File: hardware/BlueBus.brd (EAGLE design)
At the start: 64.4 x 66 mm, 46 parts

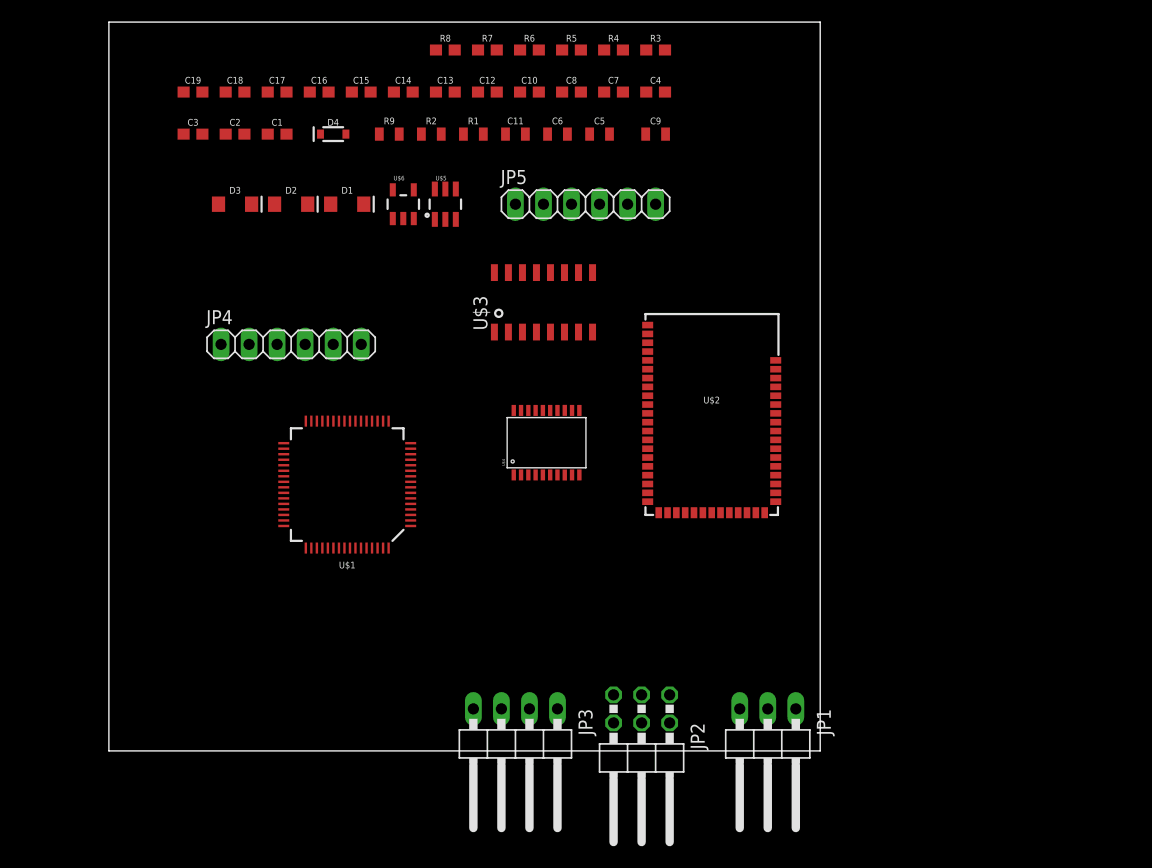
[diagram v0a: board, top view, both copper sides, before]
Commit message: [IMP] hardware: Finalize Schematic & Rev 1 board * Finish Schematic * Finalize board layout for rev 1 board
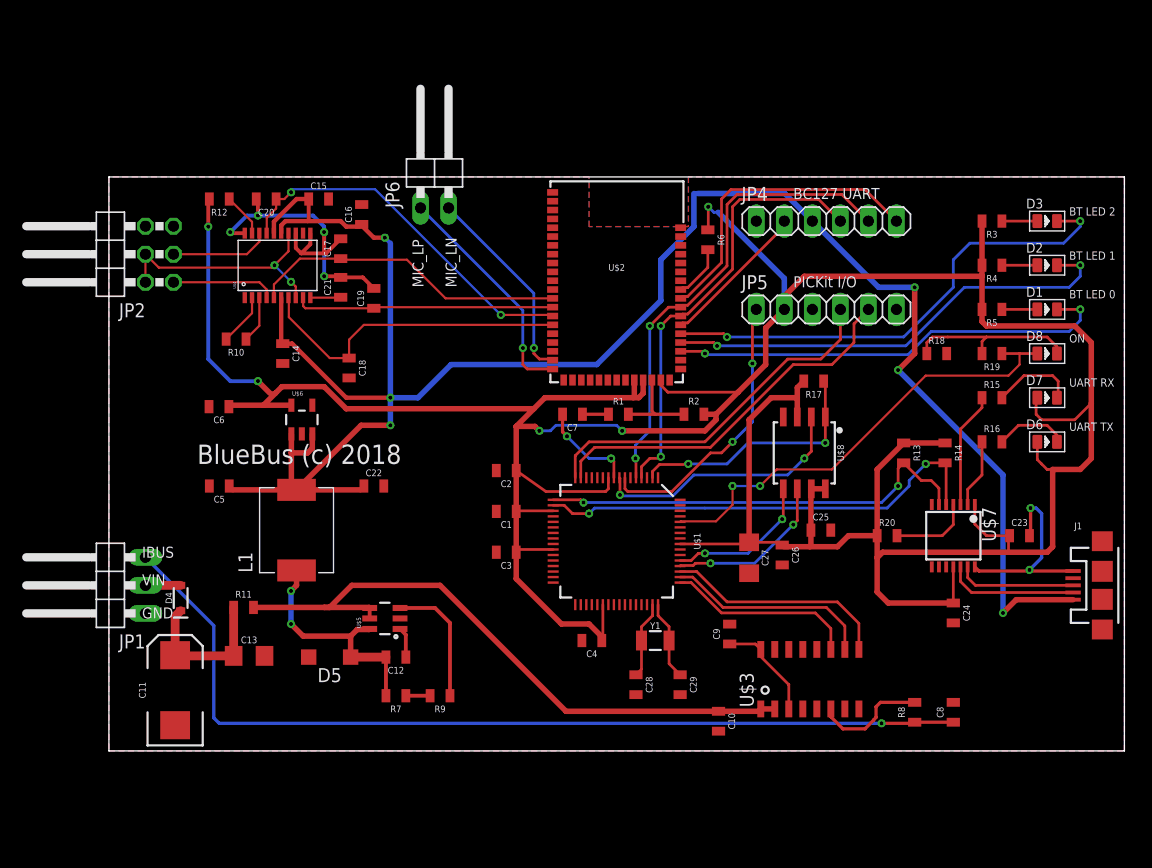
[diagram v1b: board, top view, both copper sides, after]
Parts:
- removed FRAME4: FRAME-LETTER, Frame:DUMMY
- removed JP3: (no value), pinhead:1X04/90
- added C20, C21: 0.47uF, Passives:0805
- added C22: 22uF, Passives:0805
- added C23, C24, C25, C26: 0.1uF, Passives:0805
- added C27: 10uF, Passives:1206
- added C28, C29: 18pF, Passives:0805
- added D5: 2A/30V, Passives:SOD123
- added D6: RED-0805, Seeed-LED:LED-0805
- added D7, D8: GREEN-0805, Seeed-LED:LED-0805
- added FRAME3: FRAME-LETTER, Frame:DUMMY
- added J1: (no value), SparkFun-Connectors:USB-MICROB
- added JP6: MIC_IN, pinhead:1X02/90
- added L1: 4.7uH, Passives:7.7MMX6.7MM
- added R10: 25k, Passives:0805
- added R11, R13, R14: 100k, Passives:0805
- added R12, R20: 10k, Passives:0805
- added R15, R16: 1k, Passives:0805
- added R17: 5.1k, Passives:0805
- added R18: 2k, Passives:0805
- added R19: 36k, Passives:0805
- added U$7: MCP2221A, ICs:TSSOP14
- added U$8: 512kB, ICs:SOIC-8
- added Y1: 32.768kHz, SparkFun-Clocks:CRYSTAL-SMD-3.2X1.5MM
- C1, C12, C14, C2, C3, C4, C7: device SparkFun-Capacitors:0603 -> Passives:0805
- C10: value 10nF -> 47nF; device SparkFun-Capacitors:0603 -> Passives:0805
- C11: value 10uF -> 100uF; device SparkFun-Capacitors:0805 -> Passives:EIA7343
- C13: value 0.1uF -> 10uF; device SparkFun-Capacitors:0603 -> Passives:1206
- C15, C16: value 47nF -> 0.1uF; device SparkFun-Capacitors:0603 -> Passives:0805
- C17, C18, C19: value 47nF -> 0.47uF; device SparkFun-Capacitors:0603 -> Passives:0805
- C5, C6: value 1.0uF -> 0.1uF; device SparkFun-Capacitors:0805 -> Passives:0805
- C8: value 100pF -> 0.1uF; device SparkFun-Capacitors:0603 -> Passives:0805
- C9: value 47uF/6.3V -> 2.2uF; device SparkFun-Capacitors:0805 -> Passives:0805
- D1: value BLUE -> RED-0805; device SparkFun-LED:LED-1206 -> Seeed-LED:LED-0805
- D2: value GREEN -> GREEN-0805; device SparkFun-LED:LED-1206 -> Seeed-LED:LED-0805
- D3: value RED -> CLEAR-BLUE-0805; device SparkFun-LED:LED-1206 -> Seeed-LED:LED-0805
- JP1: value (none) -> IBUS/VIN
- JP2: value (none) -> SPKR_OUT
- JP4: value (none) -> BT_FTDI
- JP5: value (none) -> MCU_PRGM
- R1, R2: device SparkFun-Resistors:0805 -> Passives:0805
- R3, R4, R5, R6, R7, R8: device SparkFun-Resistors:0603 -> Passives:0805
- R9: device Resistors:0805 -> Passives:0805
- U$4: value (none) -> TPA6012A2
- U$6: value (none) -> XC6210
- moved D3 73.6 mm to (85.0, 48.0)
- moved R8 73.5 mm to (73.0, 3.50), turned to 90 degrees
- moved D2 68.7 mm to (85.0, 44.0)
- moved JP2 67.2 mm to (-0.50, 45.0), turned to 90 degrees
- moved C8 66.0 mm to (76.5, 3.50), turned to 90 degrees
- moved D1 64.1 mm to (85.0, 40.0)
- moved JP1 62.0 mm to (-0.50, 15.0), turned to 90 degrees
- moved C10 59.5 mm to (55.2, 2.69), turned to 270 degrees
- moved R7 59.1 mm to (26.0, 5.00), turned to 180 degrees
- moved C11 59.1 mm to (6.00, 5.50), turned to 90 degrees
- moved C13 54.1 mm to (12.7, 8.61)
- moved C12 51.9 mm to (26.0, 8.50), turned to 180 degrees
- moved R9 51.1 mm to (30.0, 5.00), turned to 180 degrees
- moved C4 50.0 mm to (43.8, 10.0), turned to 180 degrees
- moved JP4 49.8 mm to (65.0, 48.0)
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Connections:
- net BT_UART_CTS renamed BT_UCTS
- net BT_UART_RTS renamed BT_URTS
- net N$1 renamed BT_VBAT_2
- net N$10 renamed FB_RES
- net N$12 renamed FB
- net N$3 renamed BT_RESET
- removed net BT_UART_RX: JP4.5, U$2.42
- removed net BT_UART_TX: JP4.4, U$2.41
- removed net IBUS_UART_RX: U$3.10
- removed net IBUS_UART_STA: U$3.9
- removed net IBUS_UART_TX: U$3.11
- removed net MIC_BIAS: U$2.17
- removed net MIC_RN: JP3.3, U$2.18
- removed net MIC_RP: JP3.1, U$2.19
- removed net N$11: C18.1, U$4.10
- removed net N$6: D1.C, U$2.38
- removed net N$7: D3.C, U$2.39
- removed net N$8: D3.A, R3.1
- removed net N$9: C10.1, U$5.1
- removed net SPKR_LN: U$2.13
- removed net SPKR_OUT_LN: JP2.2, U$4.8
- removed net SPKR_OUT_RN: JP2.4, U$4.14
- removed net VCAP: U$1.56
- removed net VCC: U$3.16
- new net BS: C12.1, U$5.1
- new net BT_URX: JP4.5, U$1.5, U$2.42
- new net BT_UTX: JP4.4, U$1.4, U$2.41
- new net BT_VBAT: R1.2, R2.1, U$2.32
- new net BYPASS: C21.1, U$4.10
- new net CRYSTAL_IN: C28.1, U$1.47, Y1.P$1
- new net CRYSTAL_OUT: C29.1, U$1.48, Y1.P$2
- new net EE_CS: R17.1, U$1.2, U$8.1
- new net EE_SCK: U$1.52, U$8.6
- new net EE_SI: U$1.53, U$8.5
- new net EE_SO: U$1.8, U$8.2
- new net GAIN0: R10.2, U$4.2
- new net GAIN1: R10.1, U$4.3
- new net IBUS_IN: R8.2, U$3.6
- new net IBUS_URX: U$1.50, U$3.10
- new net IBUS_USTA: U$1.51, U$3.9
- new net IBUS_UTX: U$1.49, U$3.11
- new net LED0: D1.-, U$2.37
- new net LED1: D2.-, U$2.38
- new net LED2: D3.-, U$2.39
- new net MCP_LED0: R16.1, U$7.2
- new net MCP_LED1: R15.1, U$7.3
- new net MCP_RESET: R20.2, U$7.4
- new net N$1: D3.+, R3.1
- new net N$3: D1.+, R5.1
- new net ON_LED: D8.+, R19.1, U$1.60
- new net ON_LED_RES: D8.-, R18.1, R19.2
- new net SHDN: R12.1, U$4.19
- new net SPKR_OUT_NEG: JP2.2, JP2.4, U$4.14, U$4.8
- new net SW: C12.2, D5.C, L1.P$1, R7.2, U$5.6
- new net SYS_URX: R14.2, U$1.18, U$7.5
- new net SYS_USB_DN: J1.D-, U$7.12
- new net SYS_USB_DP: J1.D+, U$7.13
- new net SYS_UTX: R13.2, U$1.17, U$7.6
- new net VTR: C9.1, U$3.16, U$3.3
- net 3.3V: now also C23.1, C24.1, C25.1, C26.1, C27.1, D6.+, D7.+, R12.2, R13.1, R14.1, R17.2, R20.1, U$1.56, U$2.30, U$7.1, U$7.11, U$8.3, U$8.7, U$8.8; no longer D1.A, D2.A, R4.1, R5.1, U$2.32
- net 5V: now also C15.1, C16.1, C22.1, J1.VBUS, L1.P$2; no longer C10.2, C12.1, C13.1, R7.2, U$5.6
- net GND: now also C10.2, C11.C, C20.2, C21.2, C22.2, C23.2, C24.2, C25.2, C26.2, C27.2, C28.2, C29.2, D5.A, J1.GND, R18.2, U$7.14, U$8.4; no longer C11.2, C12.2, U$3.2
- net IBUS: now also C8.1; no longer D4.A, D4.C
- net MIC_LN: now also JP6.2; no longer JP3.4
- net MIC_LP: now also JP6.1; no longer JP3.2
- net N$2: now also D2.+, R4.1; no longer R1.2, R2.1, U$2.30
- net N$4: now also D7.-, R15.2; no longer C8.1, R8.2, U$3.6
- net N$5: now also D6.-, R16.2; no longer D2.C, U$2.37
- net SPKR_IN_LN: now also C17.1, U$2.13; no longer C15.1
- net SPKR_IN_LP: now also C19.1; no longer C17.1
- net SPKR_IN_RN: now also C20.1; no longer C19.1
- net SPKR_IN_RP: now also C18.1; no longer C16.1
- net VIN: now also C10.1, C11.A, C13.1, D4.A, D4.C, R11.1, R11.2, U$3.2, U$5.4; no longer C11.1, C9.1
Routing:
- net 3.3V: track 0.00 -> 337.2 mm, vias 0 -> 5
- net 5V: track 0.00 -> 187.6 mm, vias 0 -> 6
- net IBUS: track 0.00 -> 84.4 mm, vias 0 -> 1
- net VIN: track 0.00 -> 75.4 mm
- net GND: track 0.00 -> 59.5 mm, vias 0 -> 8
- net LED2: track 0.00 -> 44.5 mm, vias 0 -> 2
- net BT_URX: track 0.00 -> 43.3 mm, vias 0 -> 2
- net LED1: track 0.00 -> 42.0 mm, vias 0 -> 2
- net ON_LED: track 0.00 -> 41.9 mm, vias 0 -> 2
- net SYS_URX: track 0.00 -> 41.8 mm, vias 0 -> 2
- net LED0: track 0.00 -> 40.7 mm, vias 0 -> 2
- net BT_UTX: track 0.00 -> 40.1 mm, vias 0 -> 2
- net SYS_UTX: track 0.00 -> 39.9 mm, vias 0 -> 2
- net MCU_PGC: track 0.00 -> 34.2 mm
- net SPKR_IN_RN: track 0.00 -> 33.8 mm, vias 0 -> 2
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- added copper zone on layer 1, net GND
- added copper zone on layer 16, net GND
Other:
- board size 64.4 x 66 mm -> 92 x 52 mm
- board text added: "BC127 UART"
- board text added: "BT LED 0"
- board text added: "BT LED 1"
- board text added: "BT LED 2"
- board text added: "BlueBus (c) 2018"
- board text added: "GND"
- board text added: "IBUS"
- board text added: "MIC_LN"
- board text added: "MIC_LP"
- board text added: "ON"
- board text added: "PICKit I/O"
- board text added: "UART RX"
- board text added: "UART TX"
- board text added: "VIN"

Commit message: [IMP] hardware: Minor updates to design * Increase trace size to 0.22mm minimum * Increase all power traces to .5mm minimum * Add silkscreen goodies and name parts directly on PCB * Ensure all nets are named aptly
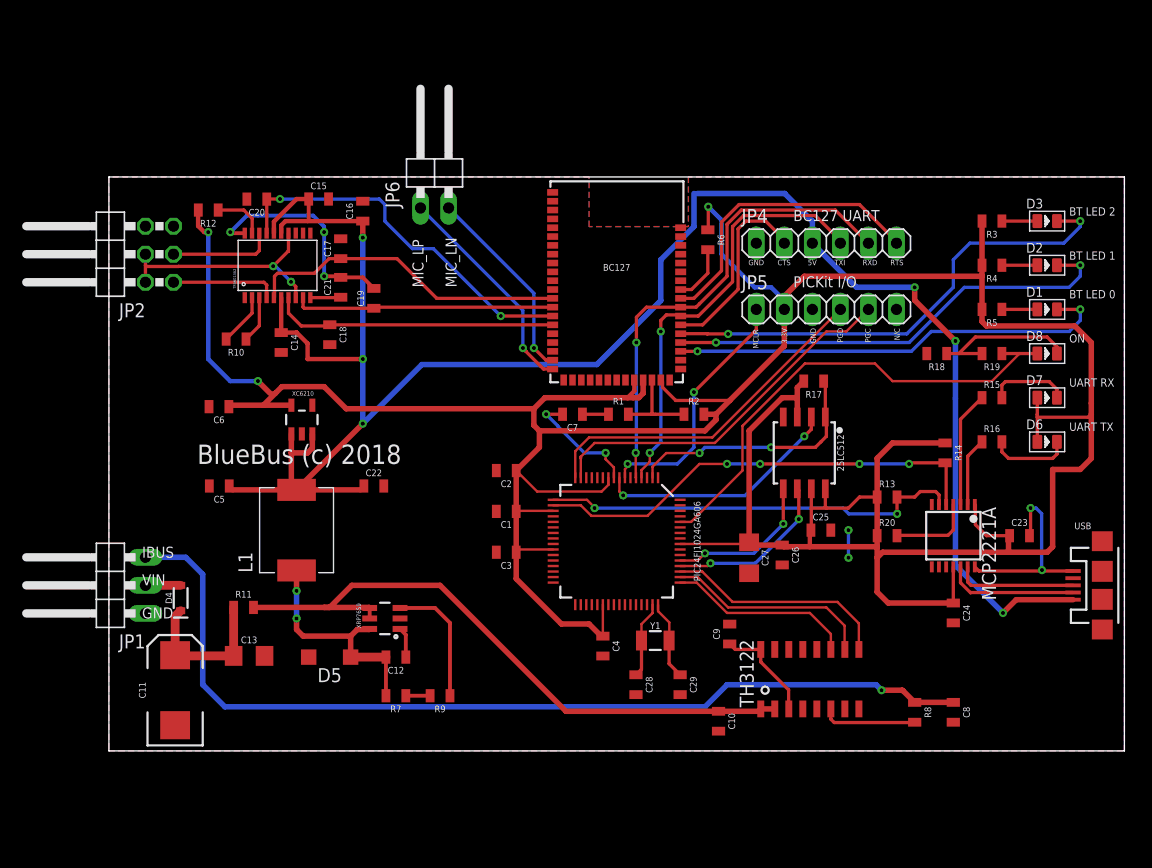
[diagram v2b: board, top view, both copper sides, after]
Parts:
- moved R13 4.27 mm to (70.5, 23.0), turned to 0 degrees
- moved C18 3.49 mm to (20.0, 37.7)
- moved JP4 2.00 mm to (65.0, 46.0)
- moved R12 1.41 mm to (9.00, 49.0)
- moved C4 1.12 mm to (44.8, 9.50), turned to 270 degrees
- moved C14 1.01 mm to (15.6, 37.0)
- moved C20 0.85 mm to (13.4, 50.0)
- moved C16 0.32 mm to (23.0, 48.9)
- turned C8 to 270 degrees
- turned R18 to 180 degrees
- turned R8 to 270 degrees
- renumbered J1 to USB, U$1 to PIC24FJ1024GA606, U$2 to BC127, U$3 to TH3122, U$4 to TPA6013A2, U$5 to XRP7659, U$6 to XC6210, U$7 to MCP2221A, U$8 to 25LC512
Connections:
- net N$1 renamed LED2_RES
- net N$2 renamed LED1_RES
- net N$3 renamed LED0_RES
- net N$4 renamed MCP_LED1_RES
- net N$5 renamed MCP_LED0_RES
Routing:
- net GND: track 59.5 -> 51.7 mm, vias 8 -> 9
- net 5V: track 187.6 -> 183.1 mm
- net BT_UCTS: track 13.6 -> 17.5 mm
- net SPKR_IN_RP: track 29.4 -> 25.9 mm
- net 3.3V: track 337.2 -> 340.5 mm, vias 5 -> 3
- net MCU_MCLR: track 25.6 -> 22.8 mm
- net ON_LED: track 41.9 -> 44.0 mm, vias 2 -> 0
- net ON_LED_RES: track 15.6 -> 13.7 mm
- net IBUS: track 84.4 -> 86.1 mm
- net IBUS_IN: track 10.3 -> 8.66 mm
- net SYS_UTX: track 39.9 -> 38.3 mm
- net MCU_PGD: track 33.1 -> 31.7 mm
- net EE_SO: track 23.7 -> 22.4 mm
- net BT_URTS: track 28.2 -> 27.2 mm
- net MIC_LP: track 20.9 -> 20.0 mm
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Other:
- board text added: "3.3V"
- board text added: "5V"
- board text added: "CTS"
- board text added: "MCLR"
- board text added: "N/C"
- board text added: "PGC"
- board text added: "PGD"
- board text added: "RTS"
- board text added: "RXD"
- board text added: "TXI"

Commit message: [IMP] hardware: Add Diode to 5V USB Input * Add diode to prevent voltage oopsies in case someone plugs > 5VDC to the rail
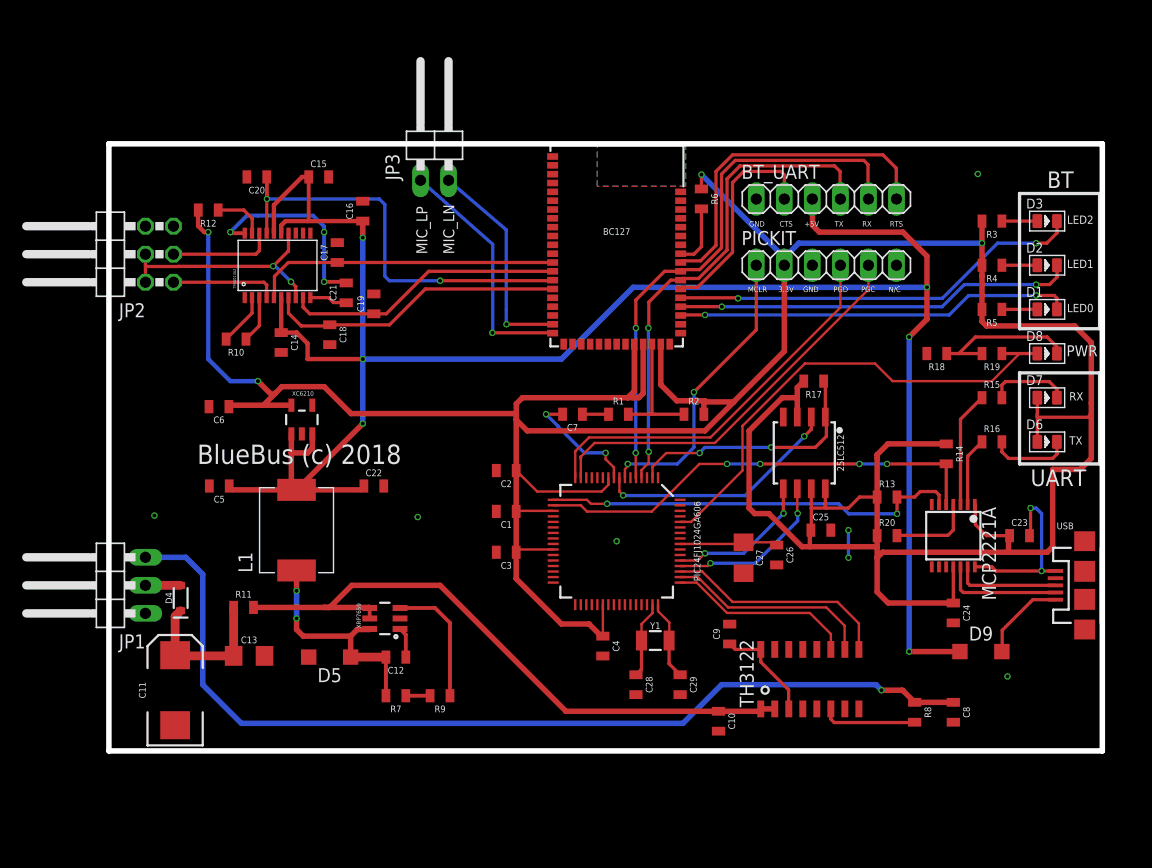
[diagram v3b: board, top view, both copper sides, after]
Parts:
- removed JP4: BT_FTDI, pinhead:1X06
- removed JP5: MCU_PRGM, pinhead:1X06
- removed JP6: MIC_IN, pinhead:1X02/90
- added BT_UART: BT_FTDI, pinhead:1X06
- added D9: 2A/30V, Passives:SOD123
- added JP3: MIC_IN, pinhead:1X02/90
- added PICKIT: MCU_PRGM, pinhead:1X06
- USB: value (none) -> USB
- moved FRAME1 3.90 mm to (45.0, 57.5)
- moved FRAME2 3.90 mm to (42.5, 57.5)
- moved FRAME3 3.89 mm to (40.0, 57.5)
- moved R6 3.75 mm to (53.7, 50.0)
- moved BC127 3.25 mm to (46.0, 45.8)
- moved C20 2.01 mm to (13.4, 52.0)
- moved C15 2.00 mm to (19.0, 52.0)
- moved USB 1.60 mm to (88.4, 15.0)
- moved C21 0.71 mm to (21.5, 41.5)
- moved C19 0.50 mm to (24.0, 40.5)
- moved C26 0.50 mm to (60.5, 17.8)
- moved C27 0.50 mm to (57.5, 17.5)
- moved C17 0.47 mm to (20.7, 45.1)
- moved R14 0.14 mm to (75.9, 26.9)
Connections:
- new net MCP_5V: D9.A, USB.VBUS
- new net VCAP: C26.1, C27.1, PIC24FJ1024GA606.56
- net 3.3V: now also PICKIT.2; no longer C26.1, C27.1, JP5.2, PIC24FJ1024GA606.56
- net 5V: now also BT_UART.3, D9.C; no longer JP4.3, USB.VBUS
- net BT_UCTS: now also BT_UART.2; no longer JP4.2
- net BT_URTS: now also BT_UART.6; no longer JP4.6
- net BT_URX: now also BT_UART.5; no longer JP4.5
- net BT_UTX: now also BT_UART.4; no longer JP4.4
- net GND: now also BT_UART.1, PICKIT.3; no longer JP4.1, JP5.3
- net MCU_MCLR: now also PICKIT.1; no longer JP5.1
- net MCU_PGC: now also PICKIT.5; no longer JP5.5
- net MCU_PGD: now also PICKIT.4; no longer JP5.4
- net MIC_LN: now also JP3.2; no longer JP6.2
- net MIC_LP: now also JP3.1; no longer JP6.1
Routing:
- net VCAP: track 0.00 -> 10.1 mm
- net MCP_5V: track 0.00 -> 7.91 mm
- net LED2: track 44.3 -> 37.9 mm
- net BT_URX: track 43.6 -> 49.6 mm
- net BT_UTX: track 39.4 -> 45.2 mm
- net SPKR_IN_RN: track 34.3 -> 39.9 mm
- net LED1: track 41.8 -> 36.3 mm
- net 5V: track 183.1 -> 188.2 mm
- net LED0: track 40.5 -> 36.0 mm
- net 3.3V: track 340.5 -> 344.6 mm, vias 3 -> 4
- net MCU_MCLR: track 22.8 -> 26.8 mm
- net GND: track 51.7 -> 47.7 mm, vias 9 -> 14
- net MCU_PGD: track 31.7 -> 35.6 mm
- net BT_URTS: track 27.2 -> 30.8 mm
- net BT_VBAT: track 8.15 -> 11.4 mm
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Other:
- board size 92 x 52 mm -> 90 x 55 mm
- board text added: "+5V"
- board text added: "BT"
- board text added: "L+"
- board text added: "L-"
- board text added: "LED0"
- board text added: "LED1"
- board text added: "LED2"
- board text added: "PWR"
- board text added: "R+"
- board text added: "R-"
- board text added: "RX"
- board text added: "TX"
- board text added: "UART"
- board text removed: "5V"
- board text removed: "BC127 UART"
- board text removed: "BT LED 0"
- board text removed: "BT LED 1"
- board text removed: "BT LED 2"
- board text removed: "ON"
- board text removed: "PICKit I/O"
- board text removed: "RXD"
- board text removed: "TXI"
- board text removed: "UART RX"
- board text removed: "UART TX"

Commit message: [ADD] hardware: Update Schematic and Board * Remove local libraries that can be found by EAGLE automatically * Rewire VIN side of the board * Update D4 to be a 30V 2A Diode, instead of a 100V 250mA diode
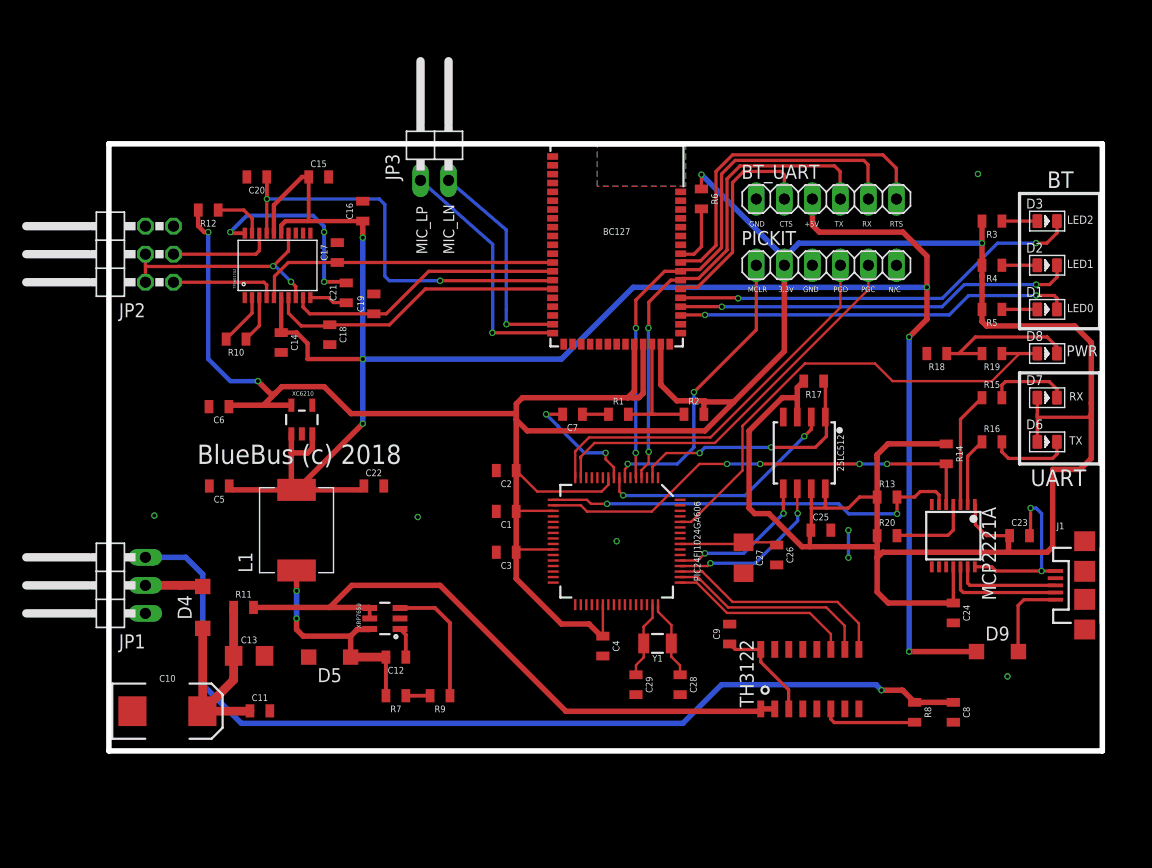
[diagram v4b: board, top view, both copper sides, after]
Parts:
- C10: value 47nF -> 100uF; device Passives:0805 -> Passives:EIA7343
- C11: value 100uF -> 47nF; device Passives:EIA7343 -> Passives:0805
- D4: value 250mA/100V -> 2A/30V; device SparkFun-DiscreteSemi:SOD-323 -> Passives:SOD123
- TPA6017A2: value TPA6012A2 -> TPA6017A2
- moved C10 49.9 mm to (5.30, 3.60), turned to 0 degrees
- moved C11 7.90 mm to (13.7, 3.63), turned to 0 degrees
- moved C28 4.00 mm to (51.8, 6.00)
- moved C29 4.00 mm to (47.8, 6.00)
- moved D4 2.17 mm to (8.50, 13.0)
- moved D9 1.50 mm to (80.5, 9.00)
- moved Y1 0.33 mm to (49.7, 9.74), turned to 180 degrees
- renumbered TPA6013A2 to TPA6017A2, USB to J1
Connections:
- net CRYSTAL_IN: now also C29.1, Y1.P$2; no longer C28.1, Y1.P$1
- net CRYSTAL_OUT: now also C28.1, Y1.P$1; no longer C29.1, Y1.P$2
- net GND: now also C10.C, C11.2; no longer C10.2, C11.C
- net VIN: now also C10.A, C11.1; no longer C10.1, C11.A
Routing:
- net VIN: track 75.4 -> 85.3 mm
- net 5V: track 188.2 -> 189.7 mm
